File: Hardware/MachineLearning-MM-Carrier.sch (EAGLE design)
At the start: 61 parts, among them J11 microSD, J2 JTAG, J3 QWIIC_RIGHT_ANGLE, J4 USB-A, J7 CAMERA-HIMAX, J9 MICROMOD-2222-C, U3 AP2127K-1.8V, U4 LIS2DH12, U5 AP7361C-33FGE

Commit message: Update MM connector. Remove backup files. Add ignore.
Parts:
- added J13: (no value), SparkFun-Connectors:I2C_STANDARD_NO_SILK
- J9: device Teensy:MICROMOD-2222-C -> SparkFun-MicroMod:MICROMOD-2222-C
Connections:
- removed net CAMERA_I2C_SCL: J7.SCL, J9.I2C_SCL1
- removed net CAMERA_I2C_SDA: J7.SDA, J9.I2C_SDA1
- removed net CAMERA_PCLK: J7.PCLK, J9.AUD_OUT
- removed net CAMERA_TRIG: J7.TRIG, J9.G8
- removed net D1: J8.6, J9.D1
- removed net I2S_SD: E2.SD, J9.AUD_IN
- new net D1/CAMERA_TRIG: J7.TRIG, J8.6, J9.D1/CAM_TRIG
- new net I2C_SCL1: J13.4, J9.I2C_SCL1
- new net I2C_SDA1: J13.3, J9.I2C_SDA1
- new net I2S_SD/CAMERA_PCLK: E2.SD, J7.PCLK, J9.AUD_IN/CAM_PCLK
- net 3.3V: now also J13.2
- net CAMERA_D0: now also J9.G0/BUS0; no longer J9.G0
- net CAMERA_D1: now also J9.G1/BUS1; no longer J9.G1
- net CAMERA_D2: now also J9.G2/BUS2; no longer J9.G2
- net CAMERA_D3: now also J9.G3/BUS3; no longer J9.G3
- net CAMERA_D4: now also J9.G4/BUS4; no longer J9.G4
- net CAMERA_D5: now also J9.G5/BUS5; no longer J9.G5
- net CAMERA_D6: now also J9.G6/BUS6; no longer J9.G6
- net CAMERA_D7: now also J9.G7/BUS7; no longer J9.G7
- net CAMERA_HSYNC: now also J9.G9/ADC_D-/CAM_HSYNC; no longer J9.G10/ADC_D+
- net CAMERA_MCLK: now also J9.AUD_OUT/CAM_MCLK; no longer J9.AUD_MCLK/CLKOUT
- net CAMERA_VSYNC: now also J9.G10/ADC_D+/CAM_VSYNC; no longer J9.G9/ADC_D-
- net GND: now also J13.1
- net I2C_SCL: now also J7.SCL
- net I2C_SDA: now also J7.SDA
- net I2S_SCK/PDM_CLK: now also J9.AUD_BCLK; no longer J9.AUD_CLK
- net I2S_WS/PDM_DAT: now also J9.AUD_LRCLK; no longer J9.AUD_DATA
- net SPI_CLK: now also J9.SPI_SCK/LED_CLK; no longer J9.LED_CLK/SPI_SCK
- net SPI_MOSI: now also J9.SPI_MOSI/LED_DAT; no longer J9.LED_DAT/SPI_MOSI
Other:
- note removed: "add DB9 for CAN bus?"
- moved on the sheet: J14, J3, JP1, R1, R4

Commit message: v11 routed
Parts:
- removed J12: (no value), SparkFun-Connectors:CONN_031X03_NO_SILK
- removed J13: (no value), SparkFun-Connectors:I2C_STANDARD_NO_SILK
- removed J4: USB-A, SparkFun-Connectors:USB_A_SMT_FEMALE
- added D2: RED, SparkFun-LED:LED-RED0603
- added JP4: JUMPER-SMT_2_NC_TRACE_SILK, SparkFun-Jumpers:JUMPER-SMT_2_NC_TRACE_SILK
- added R11: 1k, SparkFun-Resistors:1KOHM-0603-1/10W-1%
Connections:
- removed net I2C_SCL1: J13.4, J9.I2C_SCL1
- removed net I2C_SDA1: J13.3, J9.I2C_SDA1
- removed net RX2: J12.2, J9.RX2
- removed net TX2: J12.1, J9.TX2
- removed net USBHOST_D+: J4.D+, J9.USBHOST_D+
- removed net USBHOST_D-: J4.D-, J9.USBHOST_D-
- new net N$6: JP4.1, R11.2
- new net N$7: D2.A, R11.1
- net 3.3V: now also JP4.2; no longer J13.2
- net GND: now also D2.C; no longer J12.3, J13.1, J4.GND
- net V_USB: no longer J4.VBUS
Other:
- note added: "Camera IOVDD 1.8V Regulator"
- note removed: "Camera DVDD 1.8V Regulator"
- moved on the sheet: C22, H5, J1, J2, J9, R10, R2, R3, R9, S1, S2

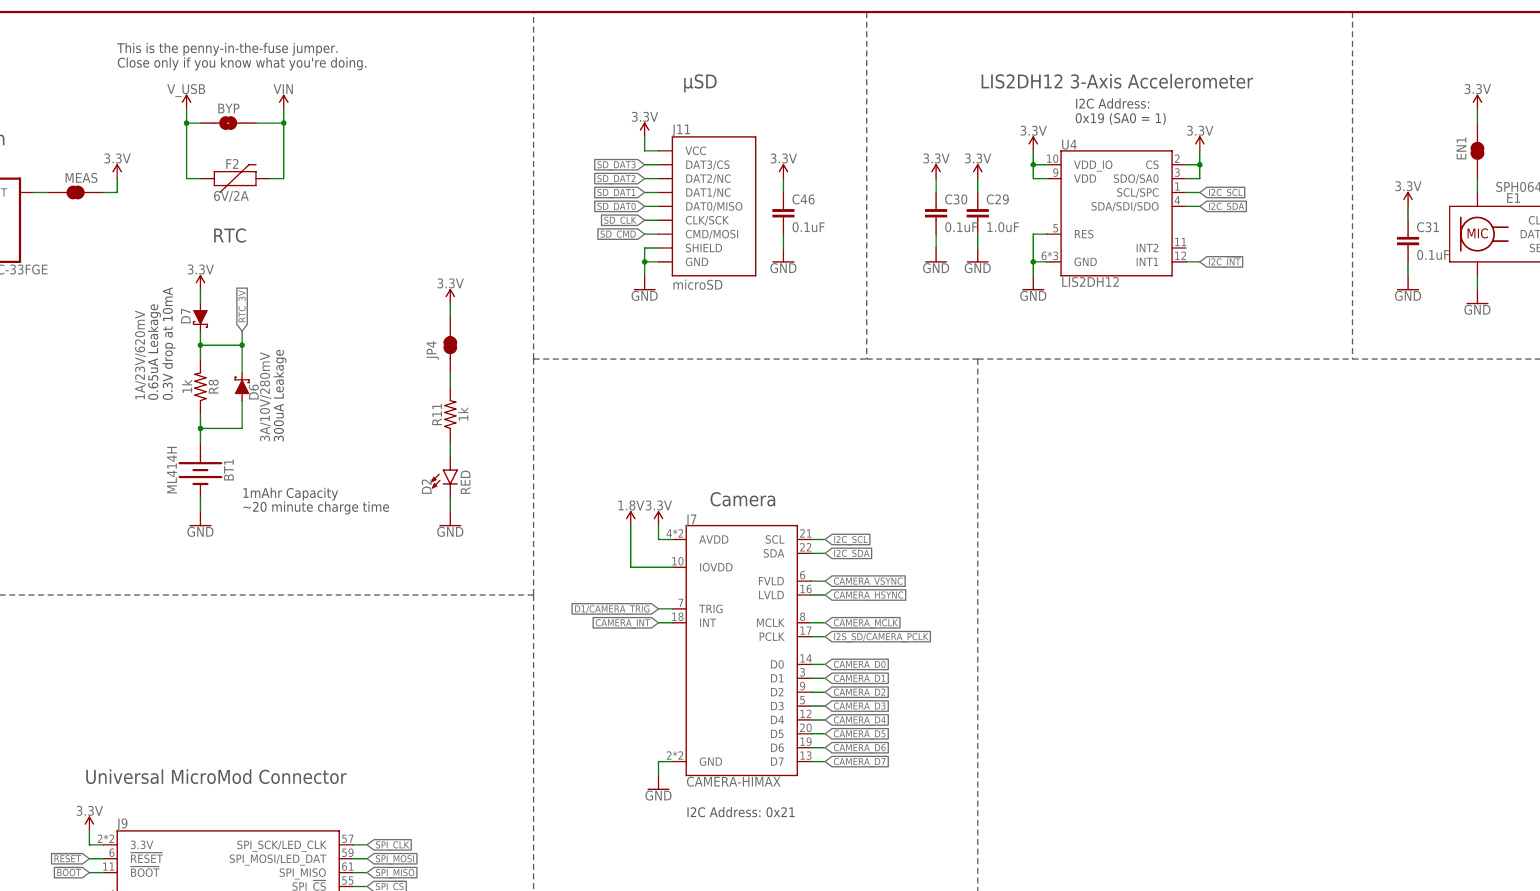
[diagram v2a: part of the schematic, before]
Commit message: Change RTC charge to 3.3k. Add bulk cap to vreg output.
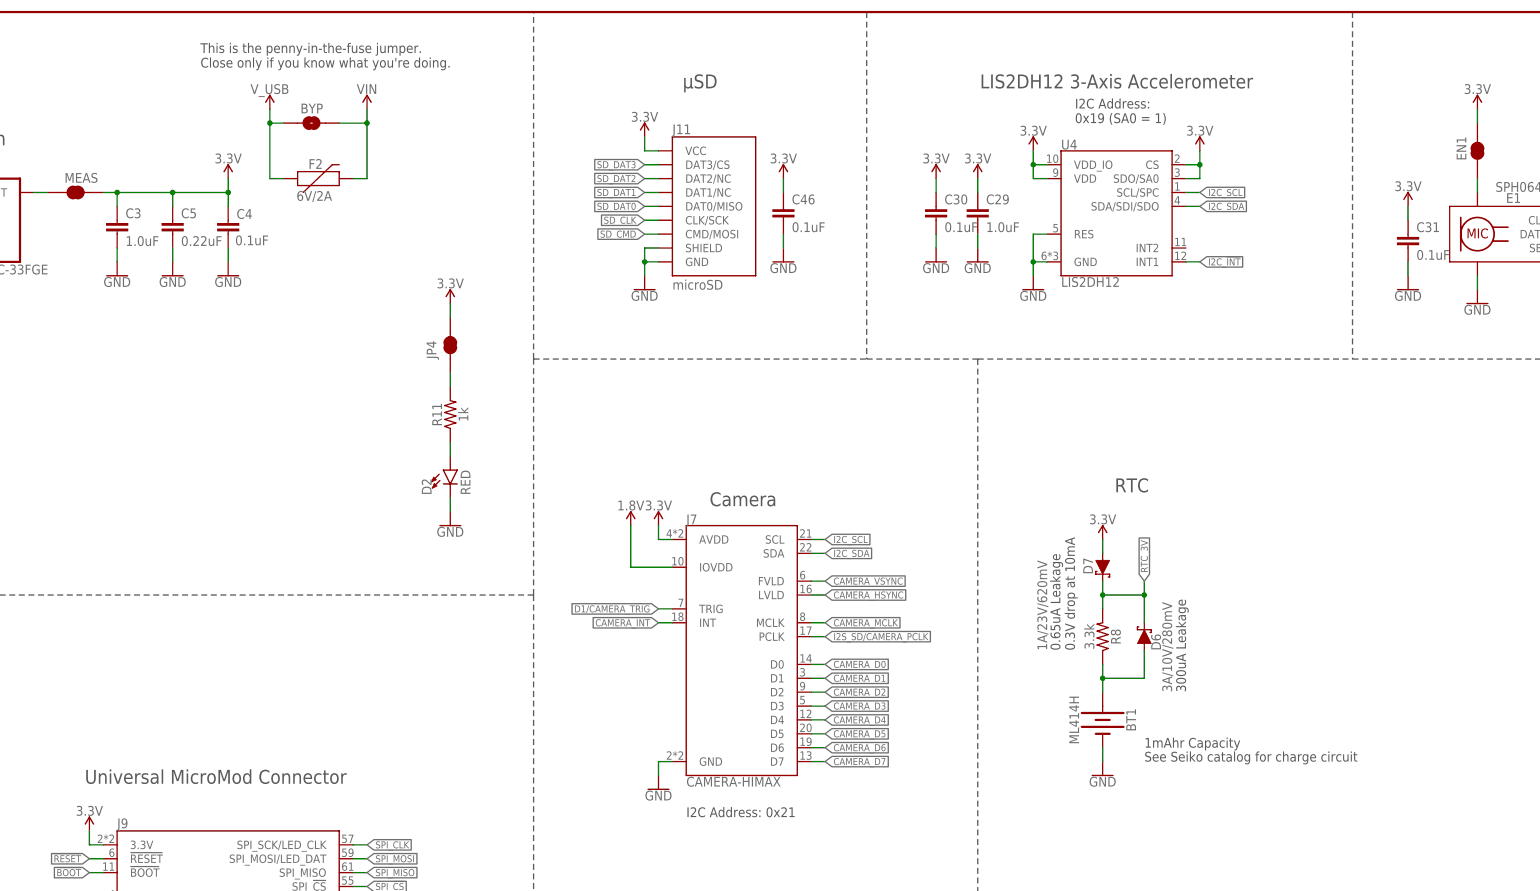
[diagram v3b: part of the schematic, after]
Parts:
- added C3: 1.0uF, SparkFun-Capacitors:1.0UF-0603-16V-10%
- added C4: 0.1uF, SparkFun-Capacitors:0.1UF-0603-25V-(+80/-20%)
- added C5: 0.22uF, SparkFun-Capacitors:0.22UF-0603-25V-10%
- R8: value 1k -> 3.3k; device SparkFun-Resistors:1KOHM-0603-1/10W-1% -> SparkFun-Resistors:3.3KOHM-0603-1/10W-1%
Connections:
- net 3.3V: now also C3.1, C4.1, C5.1
- net GND: now also C3.2, C4.2, C5.2
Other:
- note added: "See Seiko catalog for charge circuit"
- note removed: "~20 minute charge time"
- moved on the sheet: BT1, BYP, D6, D7, F2, R8

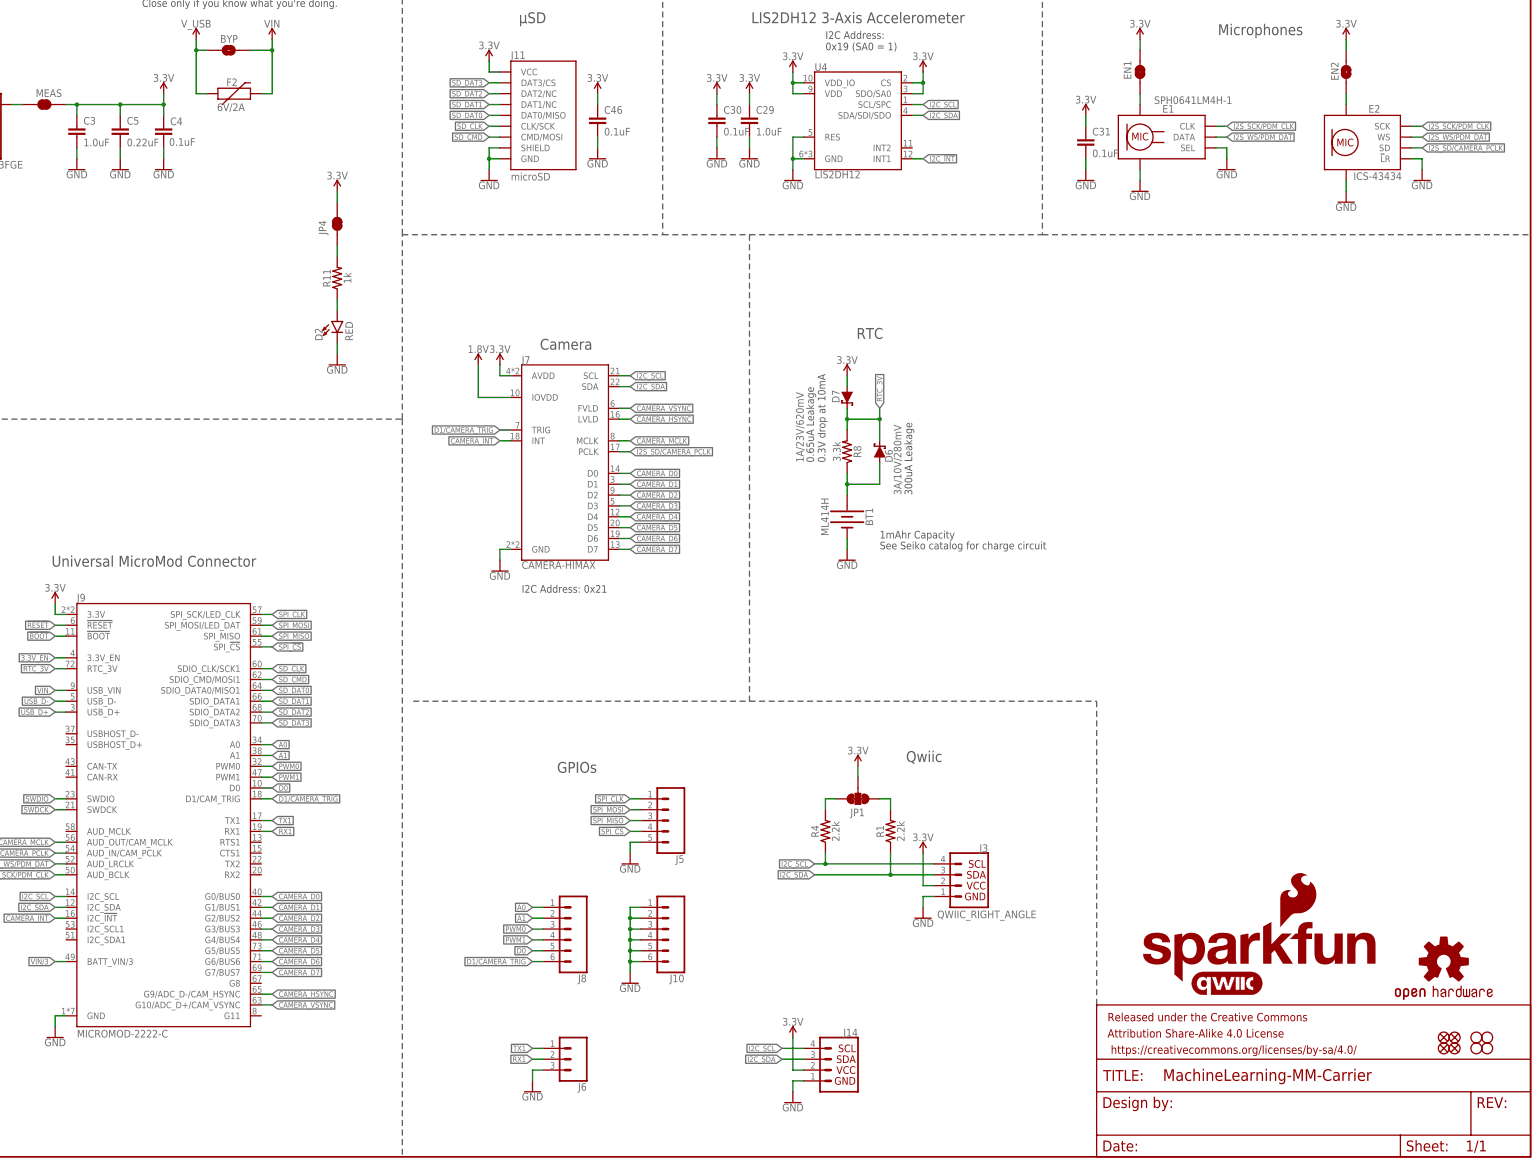
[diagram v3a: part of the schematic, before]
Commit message: Update micromod connector to new SPI pinout
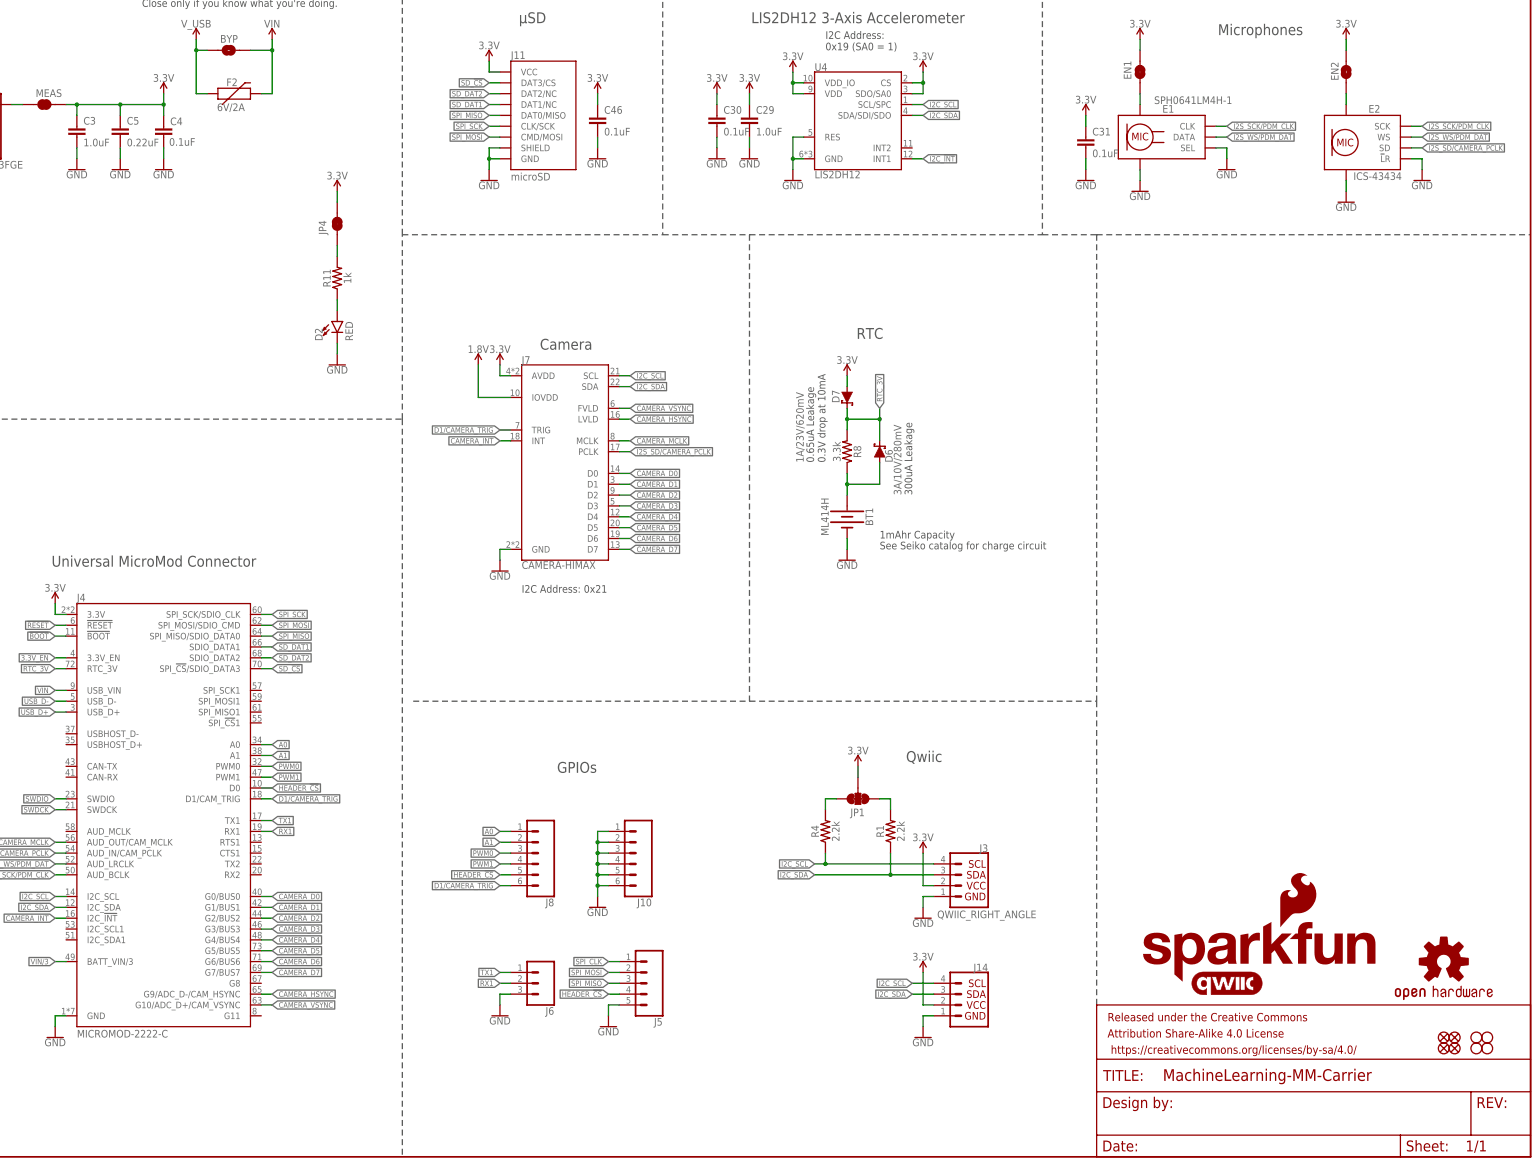
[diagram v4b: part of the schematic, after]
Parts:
- renumbered J9 to J4
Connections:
- removed net D0: J4.D0, J8.5
- removed net SD_CLK: J11.CLK/SCK, J4.SDIO_CLK/SCK1
- removed net SD_CMD: J11.CMD/MOSI, J4.SDIO_CMD/MOSI1
- removed net SD_DAT0: J11.DAT0/MISO, J4.SDIO_DATA0/MISO1
- removed net SD_DAT3: J11.DAT3/CS, J4.SDIO_DATA3
- removed net SPI_!CS!: J4.SPI_!CS!, J5.4
- new net HEADER_!CS!: J4.D0, J5.4, J8.5
- new net SD_!CS!: J11.DAT3/CS, J4.SPI_!CS!/SDIO_DATA3
- new net SPI_SCK: J11.CLK/SCK, J4.SPI_SCK/SDIO_CLK
- net SPI_CLK: no longer J4.SPI_SCK/LED_CLK
- net SPI_MISO: now also J11.DAT0/MISO, J4.SPI_MISO/SDIO_DATA0; no longer J4.SPI_MISO
- net SPI_MOSI: now also J11.CMD/MOSI, J4.SPI_MOSI/SDIO_CMD; no longer J4.SPI_MOSI/LED_DAT
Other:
- moved on the sheet: J10, J14, J5, J6, J8

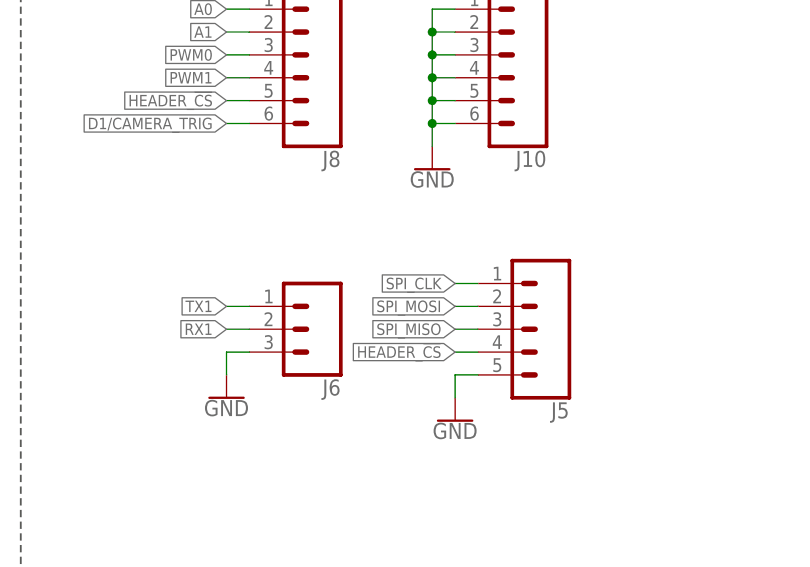
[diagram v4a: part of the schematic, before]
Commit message: Fix route to SPI SCK
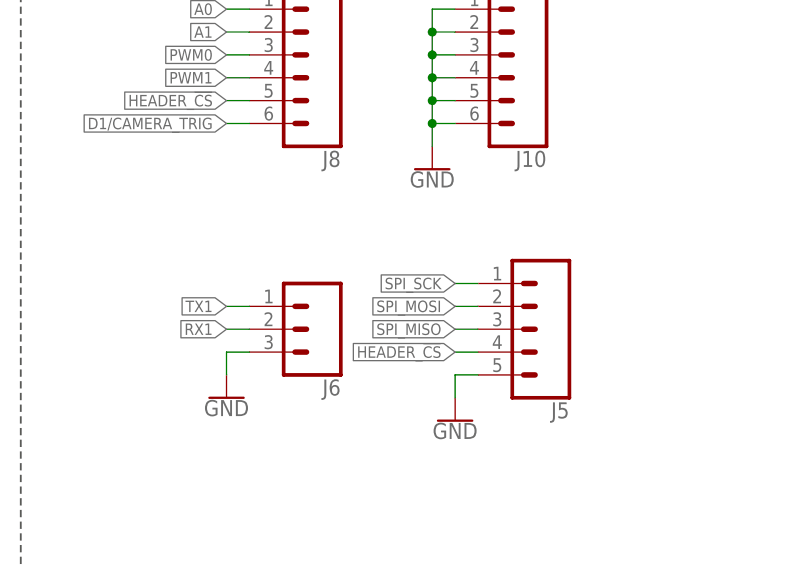
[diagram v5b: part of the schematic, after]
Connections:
- removed net SPI_CLK: J5.1
- net SPI_SCK: now also J5.1
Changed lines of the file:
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@@
 <pinref part="J4" gate="J1" pin="SPI_SCK/SDIO_CLK"/>
+</segment>
+<segment>
+<pinref part="J5" gate="G$1" pin="1"/>
+<wire x1="218.44" y1="45.72" x2="215.9" y2="45.72" width="0.1524" layer="91"/>
+<label x="215.9" y="45.72" size="1.27" layer="95" rot="R180" xref="yes"/>
 </segment>
 </net>
@@
 </segment>
 </net>
-<net name="SPI_CLK" class="0">
-<segment>
-<pinref part="J5" gate="G$1" pin="1"/>
-<wire x1="218.44" y1="45.72" x2="215.9" y2="45.72" width="0.1524" layer="91"/>
-<label x="215.9" y="45.72" size="1.27" layer="95" rot="R180" xref="yes"/>
-</segment>
-</net>

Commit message: Update v-reg device
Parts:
- U5: device ublox:AP7361C-33FGE -> SparkFun-IC-Power:AP7361C-33FGEUDFN-8
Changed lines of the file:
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@@
 <part name="GND10" library="SparkFun-PowerSymbols" deviceset="GND" device=""/>
 <part name="SUPPLY5" library="SparkFun-PowerSymbols" deviceset="V_USB" device=""/>
-<part name="U5" library="ublox" deviceset="AP7361C-33FGE" device=""/>
+<part name="U5" library="SparkFun-IC-Power" deviceset="AP7361C-33FGE" device="UDFN-8" value="AP7361C-33FGE"/>
 <part name="SUPPLY6" library="SparkFun-PowerSymbols" deviceset="3.3V" device=""/>
 <part name="GND20" library="SparkFun-PowerSymbols" deviceset="GND" device=""/>
